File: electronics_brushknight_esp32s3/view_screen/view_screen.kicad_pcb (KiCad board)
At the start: 4 copper layers, 35 x 35 mm, 14 parts, among them J1 Conn_01x04, J2 GC9A01, J3 Conn_01x04, J4 Conn_01x04, J5 Conn_01x04, J6 LCD - FPC, Q1 2N7002

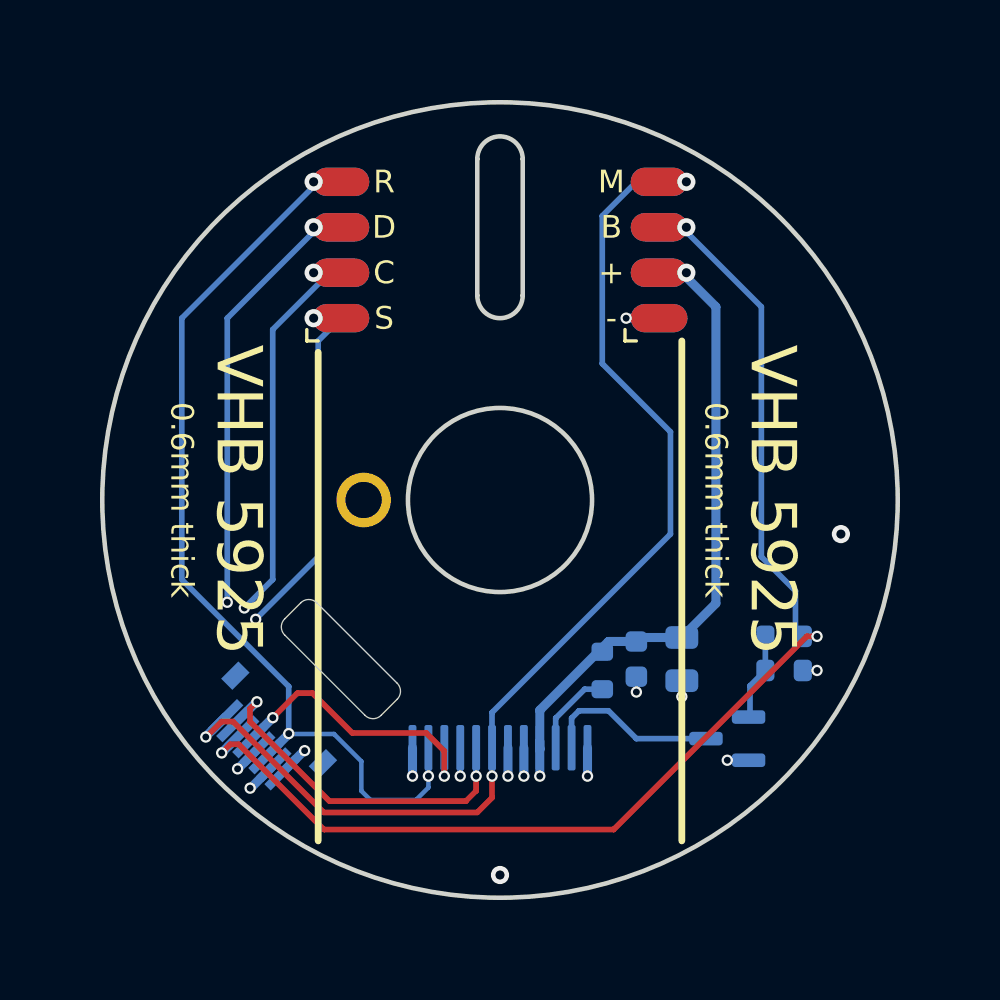
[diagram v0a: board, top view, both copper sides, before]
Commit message: Revert "DevKit PCB"
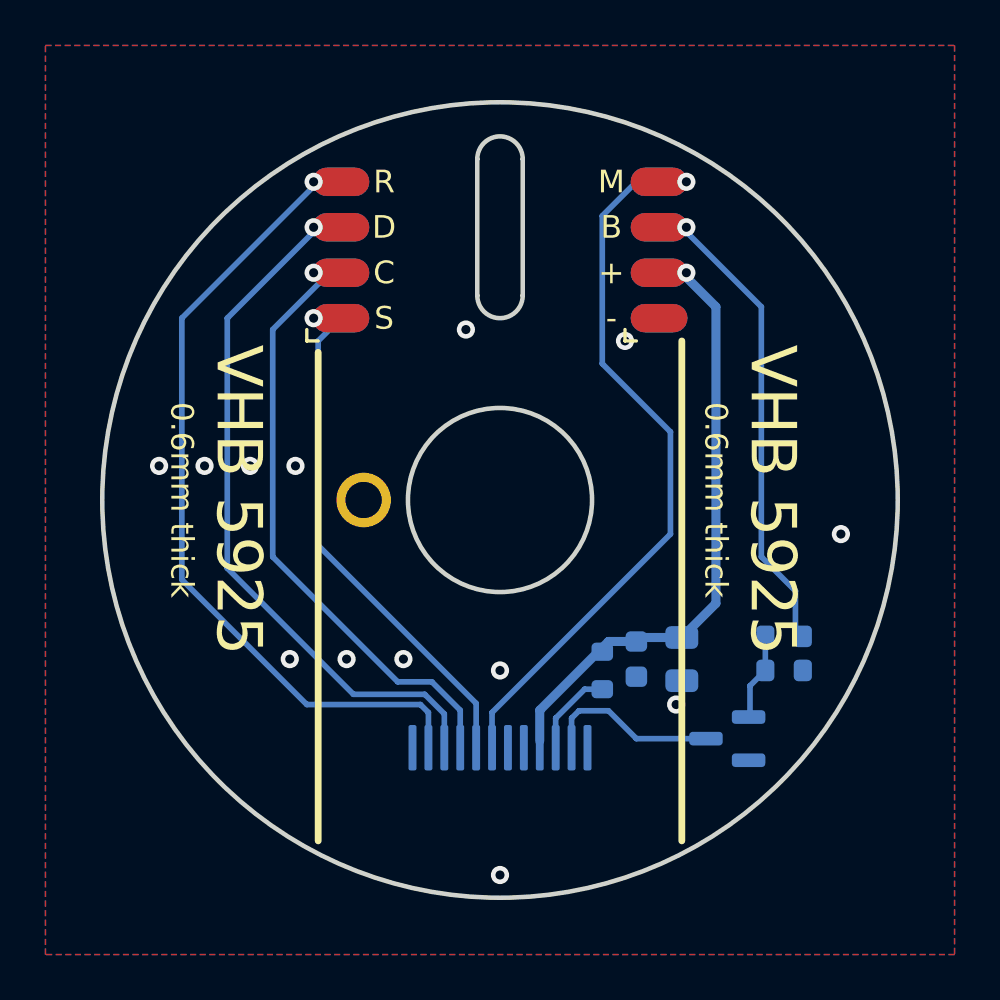
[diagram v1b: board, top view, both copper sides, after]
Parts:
- removed J6: LCD - FPC, screen_connector:Amphenol FCI FPC 8 pin 0.5 pitch
- removed REF**: fpc_wire_hole_6mm, view_custom:fpc_wire_hole_6mm
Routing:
- net /BACKLIGHT_EN: track 54.5 -> 21.2 mm, vias 3 -> 1
- net /DC: track 49.0 -> 30.7 mm, vias 3 -> 1
- net /SCK: track 39.3 -> 26.4 mm, vias 4 -> 1
- net /nCS: track 34.4 -> 21.9 mm, vias 4 -> 1
- net /MOSI: track 39.9 -> 31.0 mm, vias 4 -> 1
- net GND: track 7.92 -> 0.00 mm, vias 12 -> 13
- net /nRESET: track 41.2 -> 35.5 mm, vias 3 -> 1
- net /VDD: track 30.7 -> 27.2 mm, vias 3 -> 1
- added copper zone on B.Cu, net GND
- added copper zone on F.Cu, net GND
- removed copper zone on In1.Cu, net /VDD
- removed copper zone on In2.Cu, net GND
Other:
- copper layers 4 -> 2
- board text added: "COMMIT: ${COMMIT_HASH} DATE: ${COMMIT_DATE}"
- board text added: "Screen PCB ${RELEASE_VERSION}"
- board text removed: "Screen PCB"

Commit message: updated screen PCB
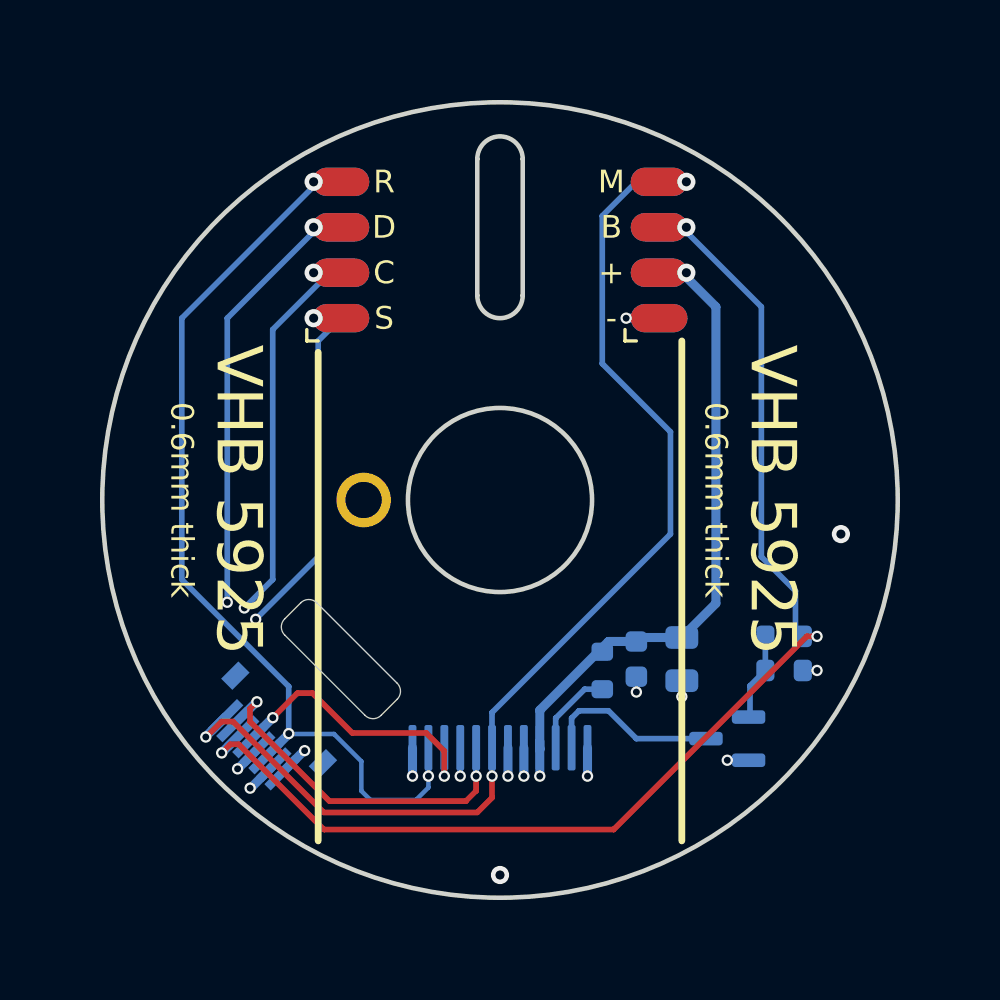
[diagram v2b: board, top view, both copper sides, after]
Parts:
- added J6: LCD - FPC, screen_connector:Amphenol FCI FPC 8 pin 0.5 pitch, B.Cu at (90.2, 109.8)
- added REF**: fpc_wire_hole_6mm, view_custom:fpc_wire_hole_6mm, F.Cu at (93.0, 107.0)
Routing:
- net /BACKLIGHT_EN: track 21.2 -> 54.5 mm, vias 1 -> 3
- net /DC: track 30.7 -> 49.0 mm, vias 1 -> 3
- net /SCK: track 26.4 -> 39.3 mm, vias 1 -> 4
- net /nCS: track 21.9 -> 34.4 mm, vias 1 -> 4
- net /MOSI: track 31.0 -> 39.9 mm, vias 1 -> 4
- net GND: track 0.00 -> 7.92 mm, vias 13 -> 12
- net /nRESET: track 35.5 -> 41.2 mm, vias 1 -> 3
- net /VDD: track 27.2 -> 30.7 mm, vias 1 -> 3
- added copper zone on In1.Cu, net /VDD
- added copper zone on In2.Cu, net GND
- removed copper zone on B.Cu, net GND
- removed copper zone on F.Cu, net GND
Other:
- copper layers 2 -> 4
- board text removed: "COMMIT: ${COMMIT_HASH} DATE: ${COMMIT_DATE}"
